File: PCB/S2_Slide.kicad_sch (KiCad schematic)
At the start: 9 parts, among them J8 10033526-N3212LF, U11 SN74LVC1T45DCK, U12 SN74LVC1T45DCK

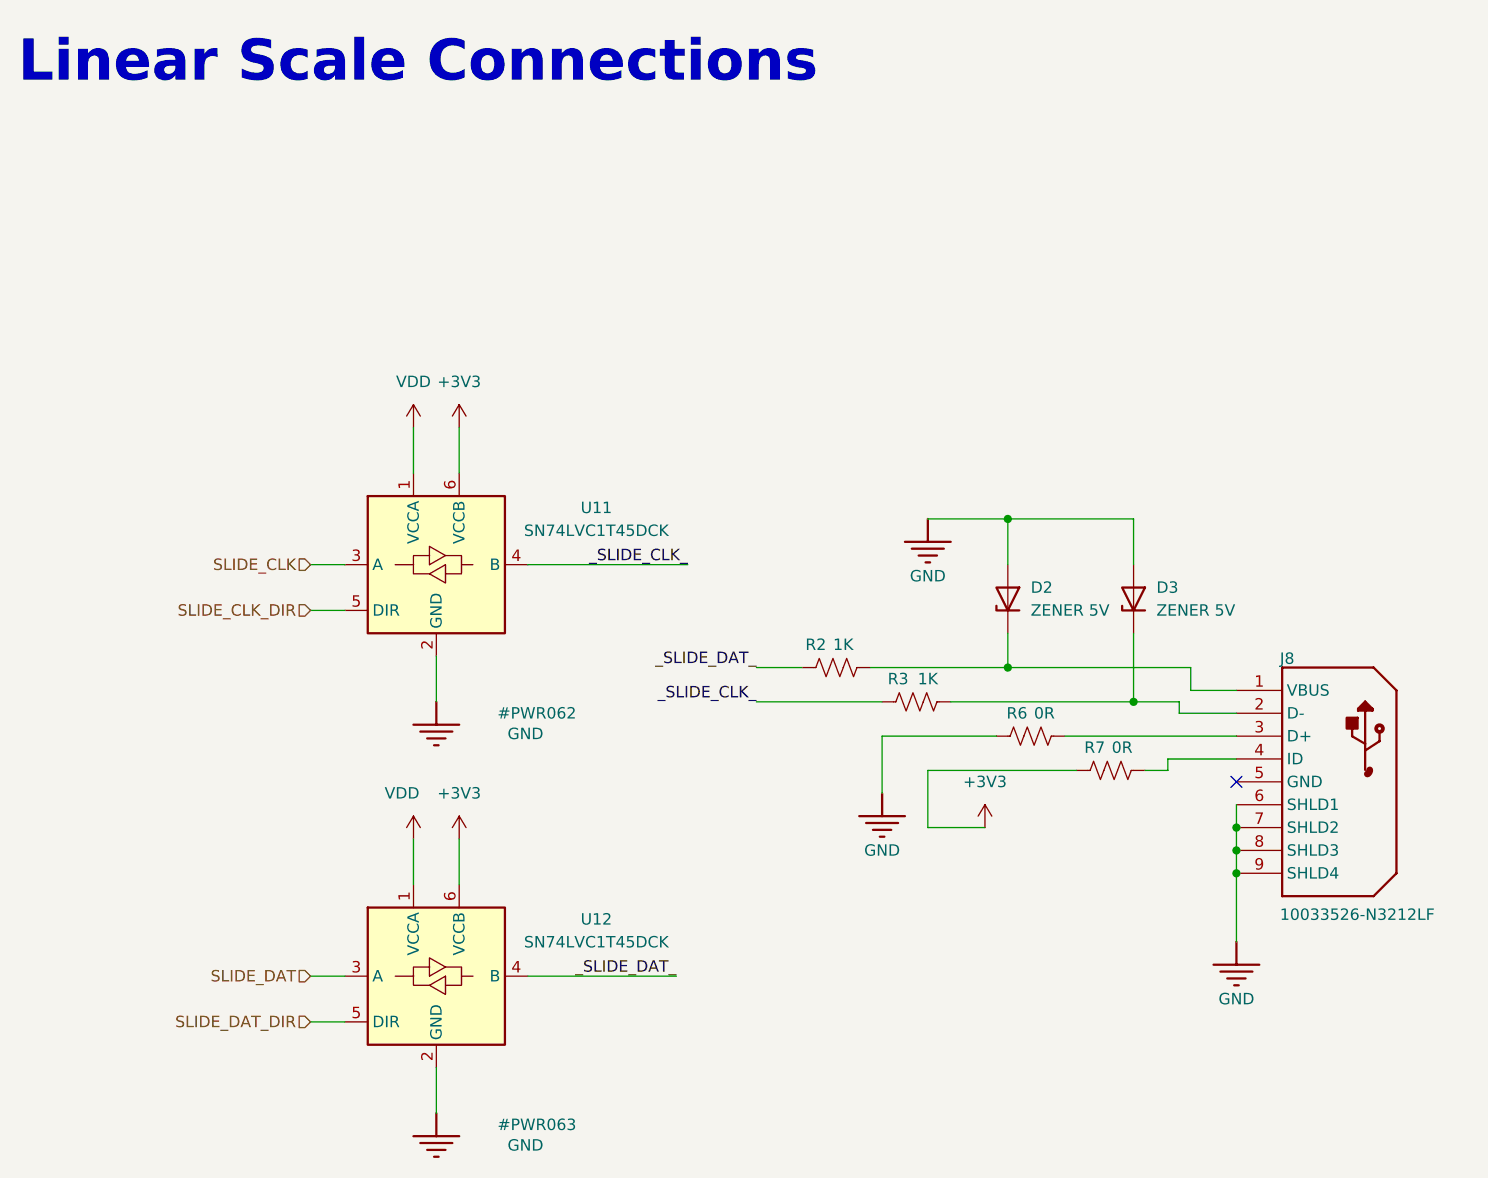
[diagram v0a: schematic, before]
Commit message: Update PCB to seperate ground symbols apporiately. Modify board to sepearte ground path for motor current and all other devices. Add filtering for slide power, hopefully reduce bownout or other issue.
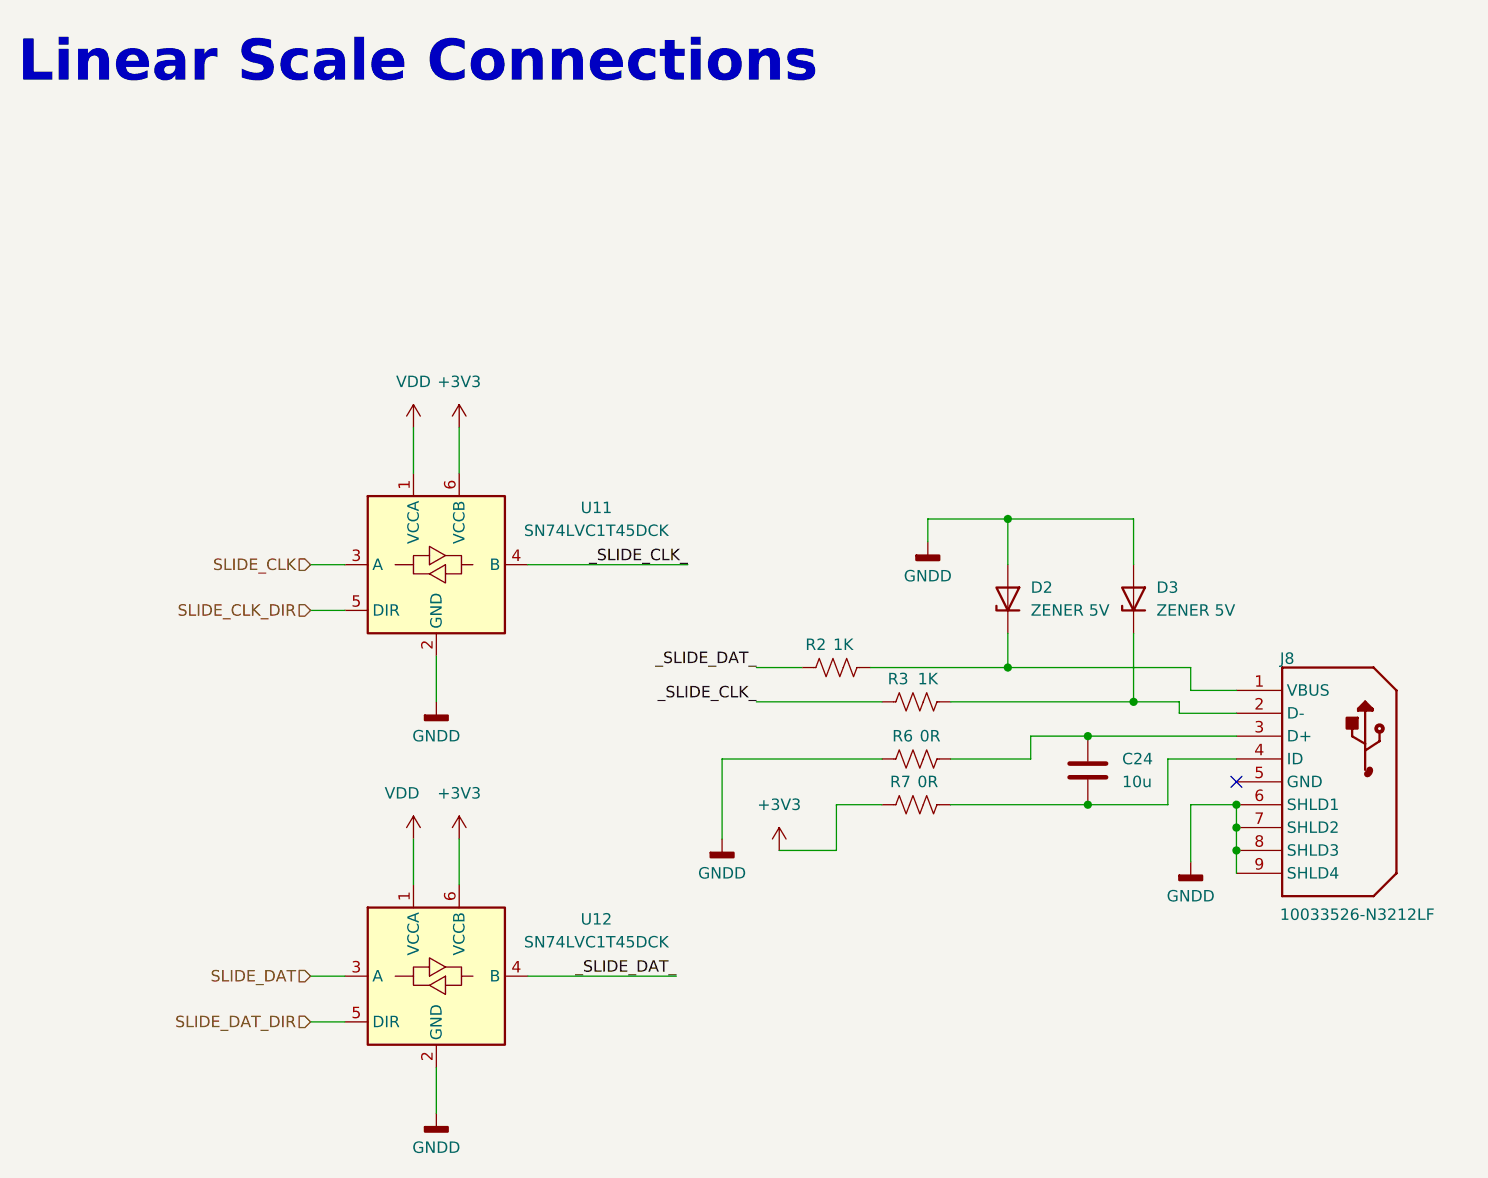
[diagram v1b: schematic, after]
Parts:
- added C24: 10u, Capacitor_SMD:C_0805_2012Metric, symbol Device:C
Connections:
- net at J8.3 (D+), R6.2: now also C24.2
- net at J8.4 (ID), R7.2: now also C24.1
- net GND renamed GNDD
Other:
- moved on the sheet: R6, R7

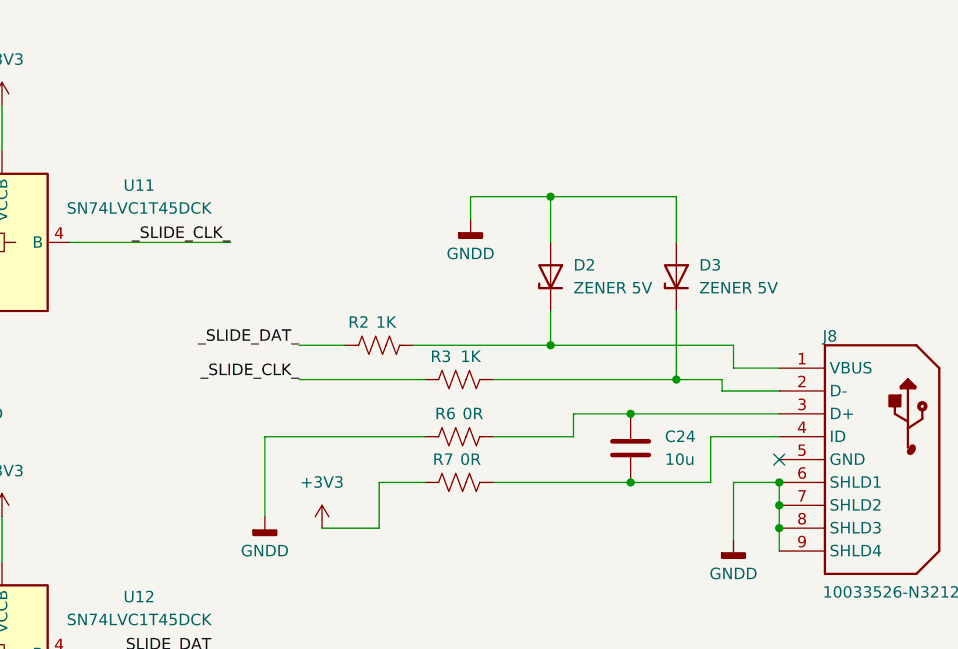
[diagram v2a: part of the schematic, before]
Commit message: Schematic bit done for adding arduino, improved motor maybe a bit by adding caps, improved slide a bit by adding protection and more caps
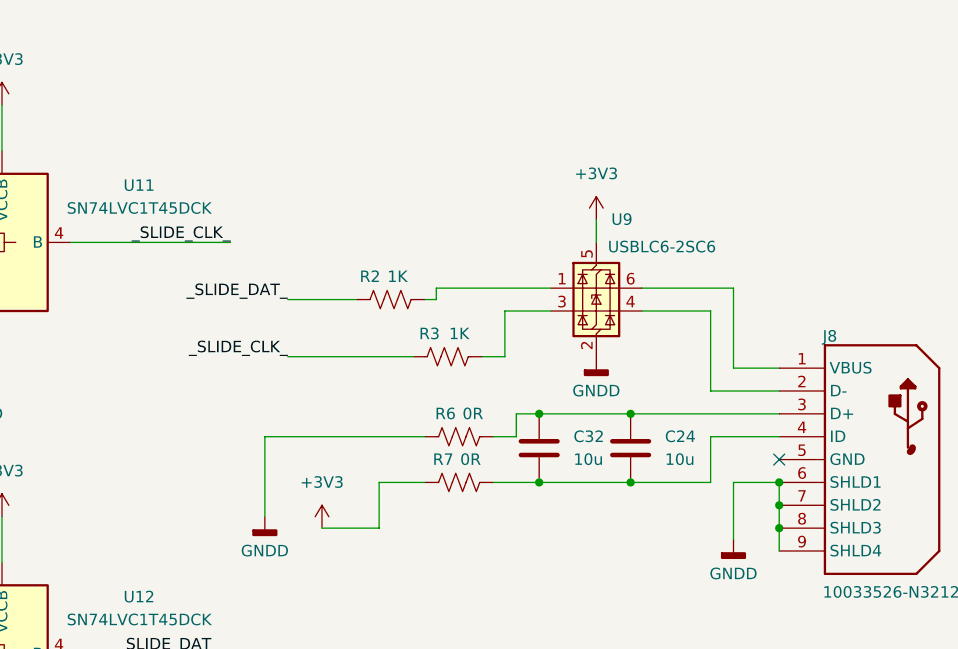
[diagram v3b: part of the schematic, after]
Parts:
- removed D2, D3: ZENER 5V, Diode_SMD:D_SOD-523, symbol Diode:ESD5Zxx
- added C32: 10u, Capacitor_SMD:C_0805_2012Metric, symbol Device:C
- added U9: USBLC6-2SC6, Package_TO_SOT_SMD:SOT-23-6, symbol Power_Protection:USBLC6-2SC6
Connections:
- net +3V3: now also U9.5 (VBUS)
- net GNDD: now also U9.2 (GND)
- net at C24.1, J8.4 (ID), R7.2: now also C32.1
- net at C24.2, J8.3 (D+), R6.2: now also C32.2
- net at J8.1 (VBUS): now also U9.6 (I/O1); no longer R2.2
- net at J8.2 (D-): now also U9.4 (I/O2); no longer R3.2
- new net: R2.2, U9.1 (I/O1)
- new net: R3.2, U9.3 (I/O2)
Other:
- moved on the sheet: R2, R3

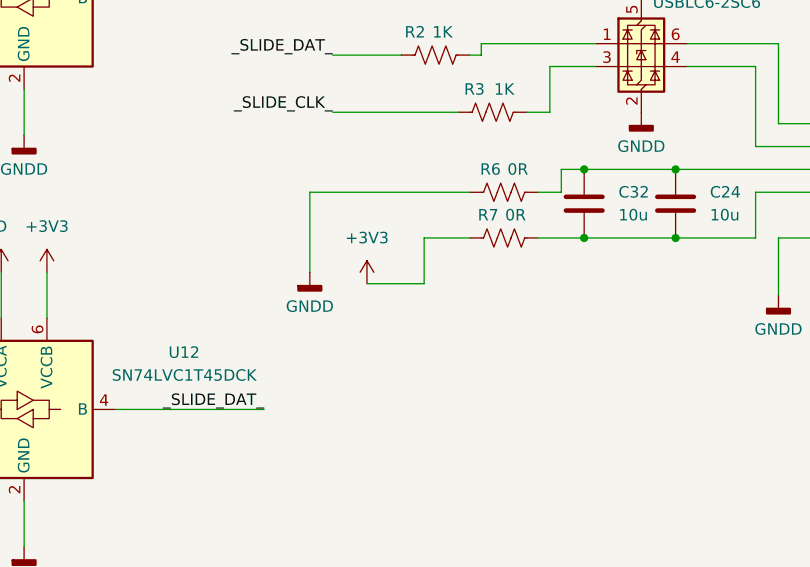
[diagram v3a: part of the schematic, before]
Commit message: Changed power stage, there as a mistake, also generally changing lots of stuff
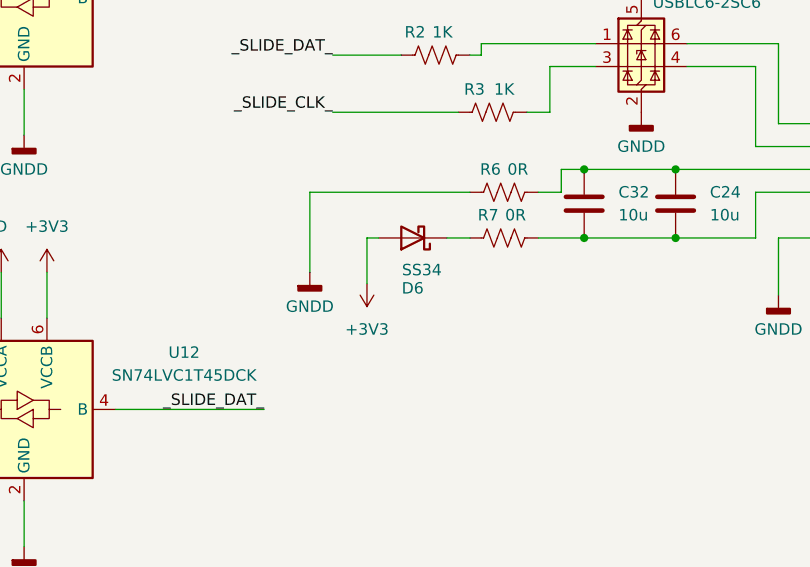
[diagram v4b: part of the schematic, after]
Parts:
- added D6: SS34, Diode_SMD:D_SMA, symbol Diode:SS34
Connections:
- net +3V3: now also D6.2 (A); no longer R7.1
- new net: D6.1 (K), R7.1
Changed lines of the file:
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@@
+	(wire
+		(pts
+			(xy 102.87 110.49) (xy 104.14 110.49)
+		)
+		(stroke
+			(width 0)
+			(type default)
+		)
+	)
 	(wire
 		(pts
@@
 	(wire
 		(pts
-			(xy 109.22 115.57) (xy 109.22 110.49)
-		)
-		(stroke
-			(width 0)
-			(type default)
-		)
-	)
-	(wire
-		(pts
 			(xy 128.27 91.44) (xy 123.19 91.44)
 		)
@@
 	(wire
 		(pts
+			(xy 102.87 115.57) (xy 102.87 110.49)
+		)
+		(stroke
+			(width 0)
+			(type default)
+		)
+	)
+	(wire
+		(pts
 			(xy 153.67 113.03) (xy 153.67 110.49)
 		)
@@
 	(wire
 		(pts
-			(xy 109.22 110.49) (xy 114.3 110.49)
-		)
-		(stroke
-			(width 0)
-			(type default)
-		)
-	)
-	(wire
-		(pts
 			(xy 146.05 105.41) (xy 153.67 105.41)
 		)
@@
 	(wire
 		(pts
-			(xy 102.87 115.57) (xy 109.22 115.57)
+			(xy 111.76 110.49) (xy 114.3 110.49)
 		)
 		(stroke
@@
 	(symbol
 		(lib_id "power:+3V3")
-		(at 102.87 115.57 0)
+		(at 102.87 115.57 180)
 		(unit 1)
 		(exclude_from_sim no)
@@
 		(fields_autoplaced yes)
 		(property "Reference" "#PWR018"
-			(at 102.87 119.38 0)
+			(at 102.87 111.76 0)
 			(effects
 				(font
@@
 		)
 		(property "Value" "+3V3"
-			(at 102.87 110.49 0)
+			(at 102.87 120.65 0)
 			(effects
 				(font
@@
 					(unit 1)
 				)
+			)
+		)
+	)
+	(symbol
+		(lib_id "Diode:SS34")
+		(at 107.95 110.49 180)
+		(unit 1)
+		(exclude_from_sim no)
+		(in_bom yes)
+		(on_board yes)
+		(dnp no)
+		(property "Reference" "D6"
+			(at 107.95 116.078 0)
+			(effects
+				(font
+					(size 1.27 1.27)
+				)
+			)
+		)
+		(property "Value" "SS34"
+			(at 108.966 114.046 0)
+			(effects
+				(font
+					(size 1.27 1.27)
+				)
+			)
+		)
+		(property "Footprint" "Diode_SMD:D_SMA"
+			(at 107.95 106.045 0)
+			(effects
+				(font
+					(size 1.27 1.27)
+				)
+				(hide yes)
+			)
+		)
+		(property "Datasheet" "https://www.vishay.com/docs/88751/ss32.pdf"
+			(at 107.95 110.49 0)
+			(effects
+				(font
+					(size 1.27 1.27)
+				)
+				(hide yes)
+			)
+		)
+		(property "Description" "40V 3A Schottky Diode, SMA"
+			(at 107.95 110.49 0)
+			(effects
+				(font
+					(size 1.27 1.27)
+				)
+				(hide yes)
+			)
+		)
+		(pin "1"
+		)
+		(pin "2"
+		)
+		(instances
+			(project "UMTK"
+				(path "/2bf3ea67-58b8-47b3-a768-ea6950b40edf/2a108526-cc67-4813-b443-9c33235e24c0"
+					(reference "D6")
+					(unit 1)
+				)

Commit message: Progress save, schematic done
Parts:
- removed R7: 0R, Resistor_SMD:R_0603_1608Metric, symbol Device:R_US
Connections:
- net at C24.1, C32.1, J8.4 (ID): now also D6.1 (K)
- net at J8.1 (VBUS): now also U9.4 (I/O2); no longer U9.6 (I/O1)
- net at J8.2 (D-): now also U9.6 (I/O1); no longer U9.4 (I/O2)
- net at U9.1 (I/O1): now also R3.2; no longer R2.2
- net at U9.3 (I/O2): now also R2.2; no longer R3.2
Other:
- moved on the sheet: R2, R3
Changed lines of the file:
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@@
-	(wire
-		(pts
-			(xy 148.59 88.9) (xy 148.59 97.79)
-		)
-		(stroke
-			(width 0)
-			(type default)
-		)
-	)
 	(wire
 		(pts
@@
 	(wire
 		(pts
+			(xy 125.73 91.44) (xy 128.27 91.44)
+		)
+		(stroke
+			(width 0)
+			(type default)
+		)
+	)
+	(wire
+		(pts
 			(xy 137.16 102.87) (xy 153.67 102.87)
 		)
@@
 	(wire
 		(pts
+			(xy 121.92 87.63) (xy 124.46 87.63)
+		)
+		(stroke
+			(width 0)
+			(type default)
+		)
+	)
+	(wire
+		(pts
 			(xy 153.67 115.57) (xy 153.67 113.03)
 		)
@@
 	(wire
 		(pts
-			(xy 121.92 110.49) (xy 127 110.49)
-		)
-		(stroke
-			(width 0)
-			(type default)
-		)
-	)
-	(wire
-		(pts
-			(xy 128.27 91.44) (xy 123.19 91.44)
-		)
-		(stroke
-			(width 0)
-			(type default)
-		)
-	)
-	(wire
-		(pts
 			(xy 74.93 129.54) (xy 91.44 129.54)
 		)
@@
 	(wire
 		(pts
+			(xy 148.59 88.9) (xy 148.59 100.33)
+		)
+		(stroke
+			(width 0)
+			(type default)
+		)
+	)
+	(wire
+		(pts
 			(xy 74.93 83.82) (xy 92.71 83.82)
 		)
@@
 	(wire
 		(pts
-			(xy 114.3 90.17) (xy 115.57 90.17)
-		)
-		(stroke
-			(width 0)
-			(type default)
-		)
-	)
-	(wire
-		(pts
-			(xy 115.57 88.9) (xy 128.27 88.9)
-		)
-		(stroke
-			(width 0)
-			(type default)
-		)
-	)
-	(wire
-		(pts
 			(xy 146.05 91.44) (xy 138.43 91.44)
 		)
@@
 	(wire
 		(pts
+			(xy 124.46 87.63) (xy 124.46 88.9)
+		)
+		(stroke
+			(width 0)
+			(type default)
+		)
+	)
+	(wire
+		(pts
 			(xy 67.31 68.58) (xy 67.31 73.66)
 		)
@@
 	(wire
 		(pts
+			(xy 125.73 92.71) (xy 125.73 91.44)
+		)
+		(stroke
+			(width 0)
+			(type default)
+		)
+	)
+	(wire
+		(pts
+			(xy 123.19 92.71) (xy 125.73 92.71)
+		)
+		(stroke
+			(width 0)
+			(type default)
+		)
+	)
+	(wire
+		(pts
 			(xy 137.16 110.49) (xy 146.05 110.49)
 		)
@@
 	(wire
 		(pts
-			(xy 123.19 96.52) (xy 120.65 96.52)
-		)
-		(stroke
-			(width 0)
-			(type default)
-		)
-	)
-	(wire
-		(pts
-			(xy 99.06 96.52) (xy 113.03 96.52)
+			(xy 110.49 87.63) (xy 114.3 87.63)
 		)
 		(stroke
@@
 	(wire
 		(pts
-			(xy 148.59 97.79) (xy 153.67 97.79)
+			(xy 124.46 88.9) (xy 128.27 88.9)
 		)
 		(stroke
@@
 	(wire
 		(pts
-			(xy 146.05 91.44) (xy 146.05 100.33)
+			(xy 146.05 91.44) (xy 146.05 97.79)
 		)
 		(stroke
@@
 	(wire
 		(pts
+			(xy 148.59 100.33) (xy 153.67 100.33)
+		)
+		(stroke
+			(width 0)
+			(type default)
+		)
+	)
+	(wire
+		(pts
 			(xy 127 110.49) (xy 137.16 110.49)
 		)
@@
 	(wire
 		(pts
-			(xy 115.57 90.17) (xy 115.57 88.9)
-		)
-		(stroke
-			(width 0)
-			(type default)
-		)
-	)
-	(wire
-		(pts
-			(xy 106.68 90.17) (xy 99.06 90.17)
-		)
-		(stroke
-			(width 0)
-			(type default)
-		)
-	)
-	(wire
-		(pts
-			(xy 146.05 100.33) (xy 153.67 100.33)
+			(xy 115.57 92.71) (xy 107.95 92.71)
+		)
+		(stroke
+			(width 0)
+			(type default)
+		)
+	)
+	(wire
+		(pts
+			(xy 146.05 97.79) (xy 153.67 97.79)
 		)
 		(stroke
@@
 	(wire
 		(pts
-			(xy 123.19 91.44) (xy 123.19 96.52)
-		)
-		(stroke
-			(width 0)
-			(type default)
-		)
-	)
-	(wire
-		(pts
-			(xy 111.76 110.49) (xy 114.3 110.49)
+			(xy 111.76 110.49) (xy 127 110.49)
 		)
 		(stroke
@@
 	)
 	(label "_SLIDE_CLK_"
-		(at 99.06 96.52 180)
+		(at 110.49 87.63 180)
 		(effects
 			(font
@@
 	)
 	(label "_SLIDE_DAT_"
-		(at 99.06 90.17 180)
+		(at 107.95 92.71 180)
 		(effects
 			(font
@@
 	)
 	(symbol
-		(lib_id "Device:R_US")
-		(at 118.11 110.49 90)
-		(unit 1)
-		(exclude_from_sim no)
-		(in_bom yes)
-		(on_board yes)
-		(dnp no)
-		(property "Reference" "R7"
-			(at 116.332 107.95 90)
-			(effects
-				(font
-					(size 1.27 1.27)
-				)
-			)
-		)
-		(property "Value" "0R"
-			(at 119.38 107.95 90)
-			(effects
-				(font
-					(size 1.27 1.27)
-				)
-			)
-		)
-		(property "Footprint" "Resistor_SMD:R_0603_1608Metric"
-			(at 118.364 109.474 90)
-			(effects
-				(font
-					(size 1.27 1.27)
-				)
-				(hide yes)
-			)
-		)
-		(property "Datasheet" "~"
-			(at 118.11 110.49 0)
-			(effects
-				(font
-					(size 1.27 1.27)
-				)
-				(hide yes)
-			)
-		)
-		(property "Description" "Resistor, US symbol"
-			(at 118.11 110.49 0)
-			(effects
-				(font
-					(size 1.27 1.27)
-				)
-				(hide yes)
-			)
-		)
-		(pin "1"
-		)
-		(pin "2"
-		)
-		(instances
-			(project "UMTK"
-				(path "/2bf3ea67-58b8-47b3-a768-ea6950b40edf/2a108526-cc67-4813-b443-9c33235e24c0"
-					(reference "R7")
-					(unit 1)
-				)
-			)
-		)
-	)
-	(symbol
 		(lib_id "power:GNDD")
 		(at 64.77 144.78 0)
@@
 	(symbol
 		(lib_id "Device:R_US")
-		(at 116.84 96.52 90)
+		(at 118.11 87.63 90)
 		(unit 1)
 		(exclude_from_sim no)
@@
 		(dnp no)
 		(property "Reference" "R3"
-			(at 114.808 93.98 90)
+			(at 116.078 85.09 90)
 			(effects
 				(font
@@
 		)
 		(property "Value" "1K"
-			(at 118.11 93.98 90)
+			(at 119.38 85.09 90)
 			(effects
 				(font
@@
 		)
 		(property "Footprint" "Resistor_SMD:R_0603_1608Metric"
-			(at 117.094 95.504 90)
+			(at 118.364 86.614 90)
 			(effects
 				(font
@@
 		)
 		(property "Datasheet" "~"
-			(at 116.84 96.52 0)
+			(at 118.11 87.63 0)
 			(effects
 				(font
@@
 		)
 		(property "Description" "Resistor, US symbol"
-			(at 116.84 96.52 0)
+			(at 118.11 87.63 0)
 			(effects
 				(font
@@
 	(symbol
 		(lib_id "Device:R_US")
-		(at 110.49 90.17 90)
+		(at 119.38 92.71 90)
 		(unit 1)
 		(exclude_from_sim no)
@@
 		(dnp no)
 		(property "Reference" "R2"
-			(at 108.204 87.63 90)
+			(at 117.094 90.17 90)
 			(effects
 				(font
@@
 		)
 		(property "Value" "1K"
-			(at 111.252 87.63 90)
+			(at 120.142 90.17 90)
 			(effects
 				(font
@@
 		)
 		(property "Footprint" "Resistor_SMD:R_0603_1608Metric"
-			(at 110.744 89.154 90)
+			(at 119.634 91.694 90)
 			(effects
 				(font
@@
 		)
 		(property "Datasheet" "~"
-			(at 110.49 90.17 0)
+			(at 119.38 92.71 0)
 			(effects
 				(font
@@
 		)
 		(property "Description" "Resistor, US symbol"
-			(at 110.49 90.17 0)
-			(effects
-				(font
+			(at 119.38 92.71 0)
+			(effects
+				(font
